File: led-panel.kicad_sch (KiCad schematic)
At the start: 12 parts

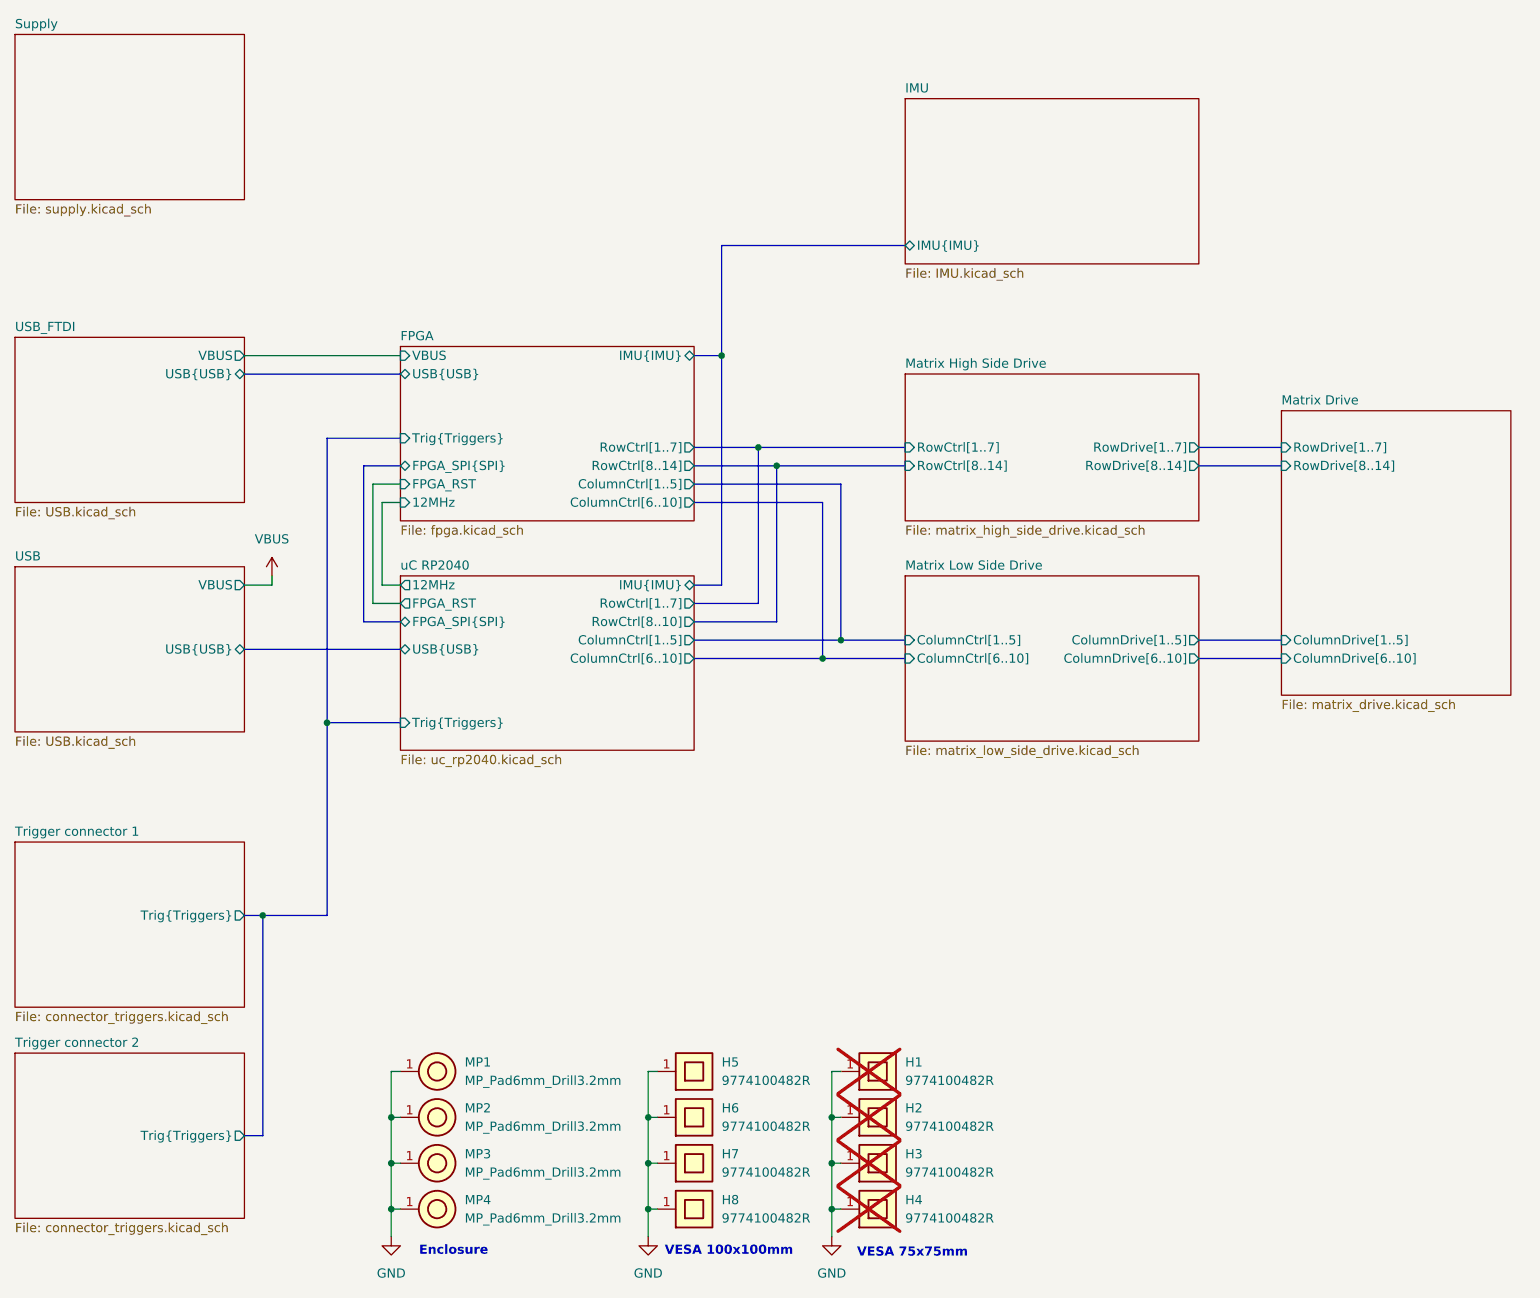
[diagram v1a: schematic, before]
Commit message: [#72133] Update USB FTDI sheet
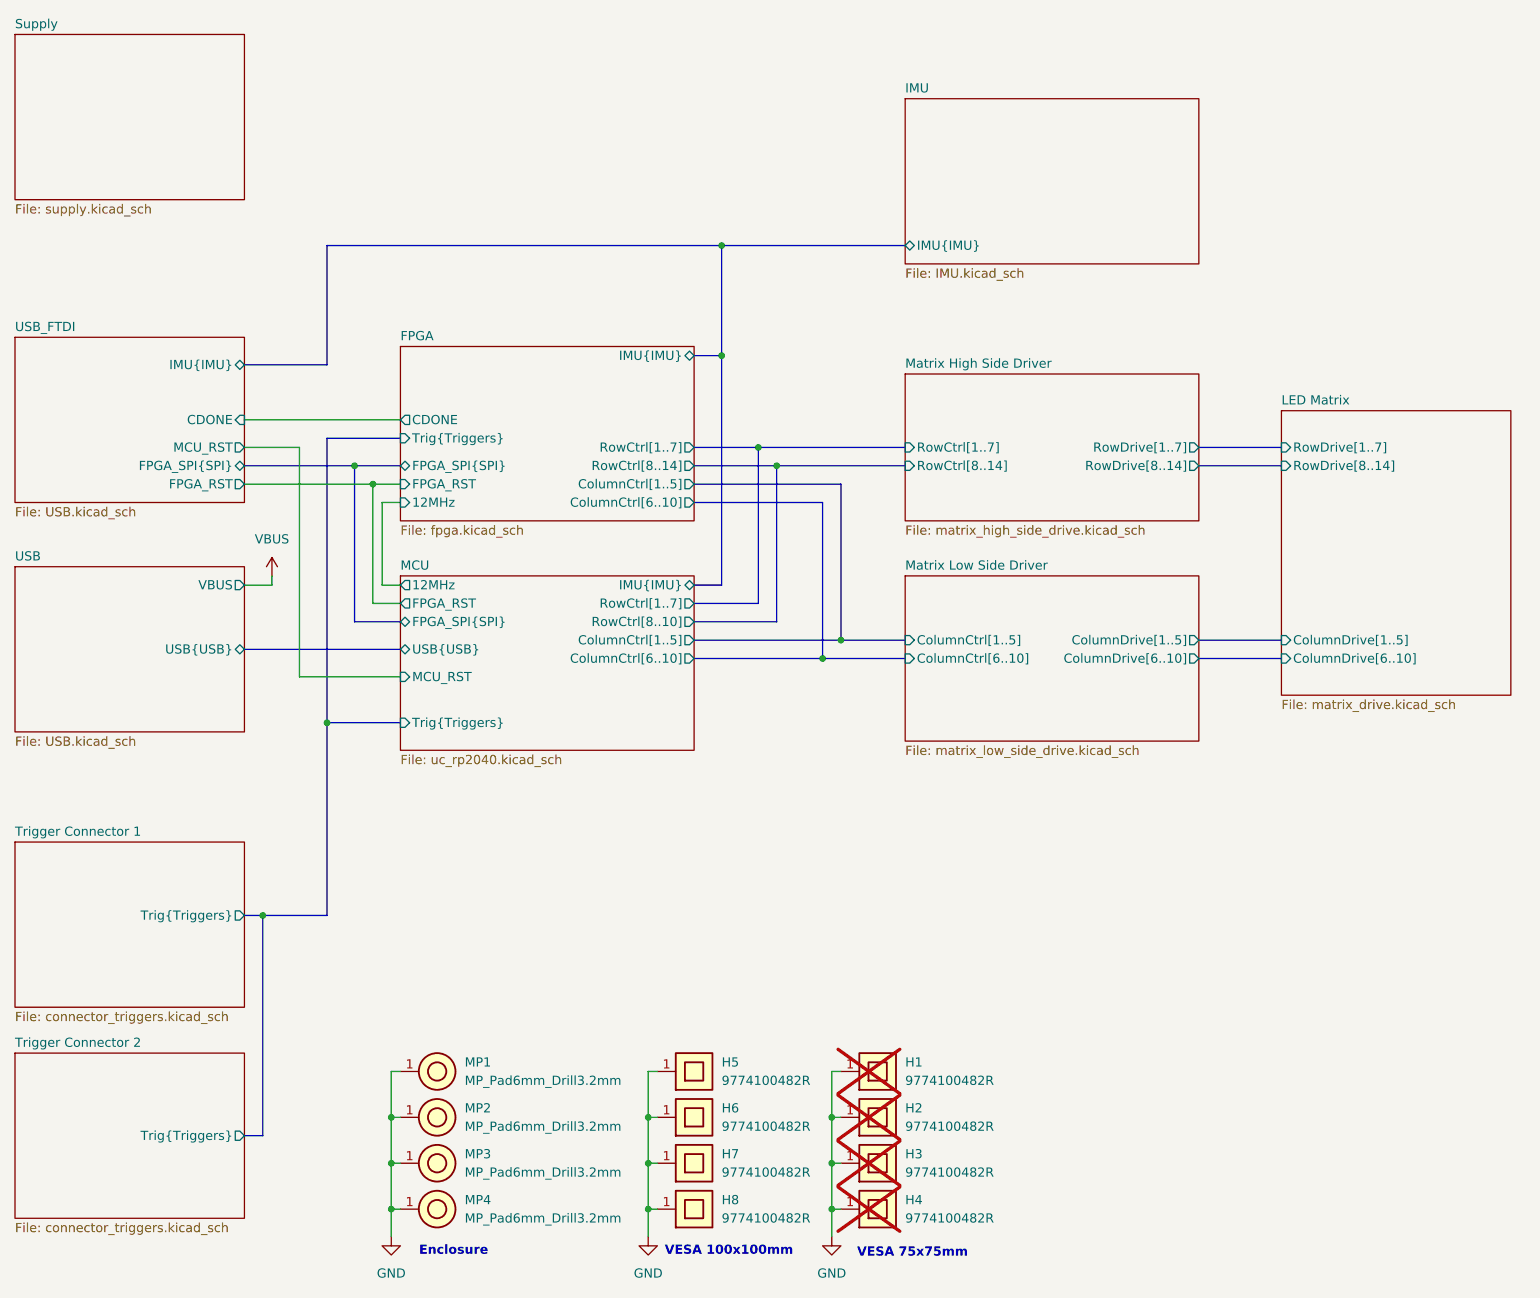
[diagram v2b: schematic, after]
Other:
- sheet Matrix Drive renamed LED Matrix
- sheet Matrix High Side Drive renamed Matrix High Side Driver
- sheet Matrix Low Side Drive renamed Matrix Low Side Driver
- sheet Trigger connector 1 renamed Trigger Connector 1
- sheet Trigger connector 2 renamed Trigger Connector 2
- sheet uC RP2040 renamed MCU
- sheet FPGA ports: added CDONE; removed USB{USB}, VBUS
- sheet MCU ports: added MCU_RST; removed none
- sheet USB_FTDI ports: added CDONE, FPGA_RST, FPGA_SPI{SPI}, IMU{IMU}, MCU_RST; removed USB{USB}, VBUS
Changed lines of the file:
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@@
 	)
 	(junction
+		(at 85.09 82.55)
+		(diameter 0)
+		(color 0 0 0 0)
+	)
+	(junction
+		(at 87.63 85.09)
+		(diameter 0)
+		(color 0 0 0 0)
+	)
+	(junction
 		(at 152.4 106.68)
 		(diameter 0)
@@
 	)
 	(junction
+		(at 135.89 52.07)
+		(diameter 0)
+		(color 0 0 0 0)
+	)
+	(junction
 		(at 125.73 185.42)
 		(diameter 0)
@@
 		)
 	)
+	(bus
+		(pts
+			(xy 69.85 68.58) (xy 81.28 68.58)
+		)
+		(stroke
+			(width 0)
+			(type default)
+		)
+	)
 	(wire
 		(pts
@@
 	(wire
 		(pts
-			(xy 69.85 67.31) (xy 91.44 67.31)
-		)
-		(stroke
-			(width 0)
-			(type default)
-		)
-	)
-	(wire
-		(pts
 			(xy 125.73 179.07) (xy 127 179.07)
 		)
@@
 		)
 	)
+	(wire
+		(pts
+			(xy 69.85 76.2) (xy 91.44 76.2)
+		)
+		(stroke
+			(width 0)
+			(type default)
+		)
+	)
 	(bus
 		(pts
@@
 	(bus
 		(pts
-			(xy 91.44 104.14) (xy 86.36 104.14)
+			(xy 91.44 104.14) (xy 85.09 104.14)
 		)
 		(stroke
@@
 	(bus
 		(pts
+			(xy 81.28 52.07) (xy 135.89 52.07)
+		)
+		(stroke
+			(width 0)
+			(type default)
+		)
+	)
+	(bus
+		(pts
 			(xy 72.39 175.26) (xy 69.85 175.26)
 		)
@@
 	(wire
 		(pts
+			(xy 69.85 85.09) (xy 87.63 85.09)
+		)
+		(stroke
+			(width 0)
+			(type default)
+		)
+	)
+	(wire
+		(pts
 			(xy 151.13 185.42) (xy 151.13 189.23)
 		)
@@
 	(bus
 		(pts
-			(xy 86.36 82.55) (xy 91.44 82.55)
+			(xy 85.09 82.55) (xy 91.44 82.55)
 		)
 		(stroke
@@
 	(wire
 		(pts
+			(xy 69.85 80.01) (xy 77.47 80.01)
+		)
+		(stroke
+			(width 0)
+			(type default)
+		)
+	)
+	(wire
+		(pts
+			(xy 77.47 111.76) (xy 91.44 111.76)
+		)
+		(stroke
+			(width 0)
+			(type default)
+		)
+	)
+	(wire
+		(pts
 			(xy 125.73 179.07) (xy 125.73 185.42)
 		)
@@
 		)
 	)
+	(bus
+		(pts
+			(xy 69.85 82.55) (xy 85.09 82.55)
+		)
+		(stroke
+			(width 0)
+			(type default)
+		)
+	)
 	(wire
 		(pts
@@
 	(bus
 		(pts
-			(xy 69.85 69.85) (xy 91.44 69.85)
+			(xy 132.08 67.31) (xy 135.89 67.31)
 		)
 		(stroke
@@
 	(bus
 		(pts
-			(xy 132.08 67.31) (xy 135.89 67.31)
+			(xy 85.09 104.14) (xy 85.09 82.55)
+		)
+		(stroke
+			(width 0)
+			(type default)
+		)
+	)
+	(wire
+		(pts
+			(xy 77.47 80.01) (xy 77.47 111.76)
 		)
 		(stroke
@@
 	(bus
 		(pts
-			(xy 86.36 104.14) (xy 86.36 82.55)
+			(xy 81.28 68.58) (xy 81.28 52.07)
 		)
 		(stroke
@@
 			(color 0 0 0 0.0000)
 		)
-		(property "Sheetname" "uC RP2040"
+		(property "Sheetname" "MCU"
 			(at 91.44 97.0784 0)
 			(effects
@@
 			)
 		)
+		(pin "MCU_RST" input
+			(at 91.44 111.76 180)
+			(effects
+				(font
+					(size 1.27 1.27)
+				)
+				(justify left)
+			)
+		)
 		(instances
 			(project "led-panel"
@@
 			(color 0 0 0 0.0000)
 		)
-		(property "Sheetname" "Trigger connector 2"
+		(property "Sheetname" "Trigger Connector 2"
 			(at 38.1 163.1184 0)
 			(effects
@@
 			(color 0 0 0 0.0000)
 		)
-		(property "Sheetname" "Matrix Drive"
+		(property "Sheetname" "LED Matrix"
 			(at 213.36 74.2184 0)
 			(effects
@@
 			(color 0 0 0 0.0000)
 		)
-		(property "Sheetname" "Trigger connector 1"
+		(property "Sheetname" "Trigger Connector 1"
 			(at 38.1 133.9084 0)
 			(effects
@@
 			(color 0 0 0 0.0000)
 		)
-		(property "Sheetname" "Matrix Low Side Drive"
+		(property "Sheetname" "Matrix Low Side Driver"
 			(at 161.29 97.0784 0)
 			(effects
@@
 			(color 0 0 0 0.0000)
 		)
-		(property "Sheetname" "Matrix High Side Drive"
+		(property "Sheetname" "Matrix High Side Driver"
 			(at 161.29 69.1384 0)
 			(effects
@@
 			)
 		)
-		(pin "USB{USB}" bidirectional
-			(at 69.85 69.85 0)
+		(pin "FPGA_SPI{SPI}" bidirectional
+			(at 69.85 82.55 0)
 			(effects
 				(font
@@
 			)
 		)
-		(pin "VBUS" output
-			(at 69.85 67.31 0)
+		(pin "IMU{IMU}" bidirectional
+			(at 69.85 68.58 0)
+			(effects
+				(font
+					(size 1.27 1.27)
+				)
+				(justify right)
+			)
+		)
+		(pin "FPGA_RST" output
+			(at 69.85 85.09 0)
+			(effects
+				(font
+					(size 1.27 1.27)
+				)
+				(justify right)
+			)
+		)
+		(pin "MCU_RST" output
+			(at 69.85 80.01 0)
+			(effects
+				(font
+					(size 1.27 1.27)
+				)
+				(justify right)
+			)
+		)
+		(pin "CDONE" input
+			(at 69.85 76.2 0)
 			(effects
 				(font
@@
 			)
 		)
-		(pin "USB{USB}" bidirectional
-			(at 91.44 69.85 180)
-			(effects
-				(font
-					(size 1.27 1.27)
-				)
-				(justify left)
-			)
-		)
 		(pin "12MHz" input
 			(at 91.44 87.63 180)
@@
 			)
 		)
-		(pin "VBUS" input
-			(at 91.44 67.31 180)
+		(pin "FPGA_RST" input
+			(at 91.44 85.09 180)
 			(effects
 				(font
@@
 			)
 		)
-		(pin "FPGA_RST" input
-			(at 91.44 85.09 180)
+		(pin "FPGA_SPI{SPI}" bidirectional
+			(at 91.44 82.55 180)
 			(effects
 				(font
@@
 			)
 		)
-		(pin "FPGA_SPI{SPI}" bidirectional
-			(at 91.44 82.55 180)
+		(pin "CDONE" output
+			(at 91.44 76.2 180)
 			(effects
 				(font

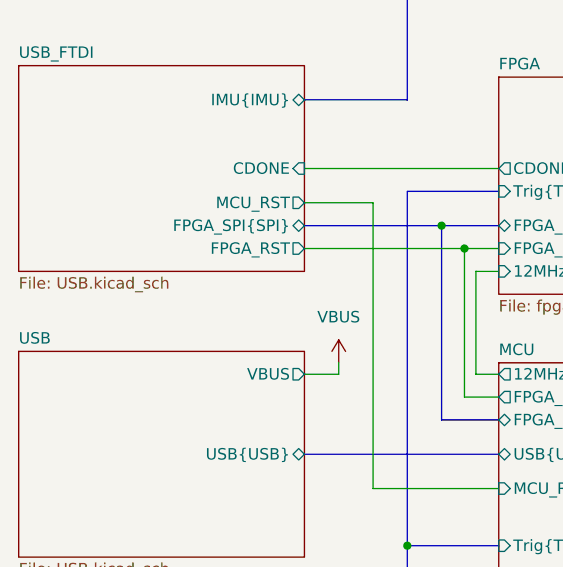
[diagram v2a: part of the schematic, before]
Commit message: [#72133] Update USB sheets
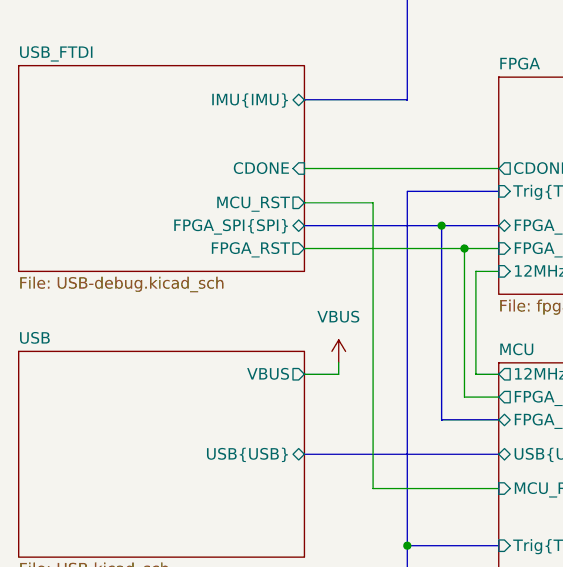
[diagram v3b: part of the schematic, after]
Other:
- sheet USB_FTDI: file USB.kicad_sch -> USB-debug.kicad_sch
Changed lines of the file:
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@@
 			)
 		)
-		(property "Sheetfile" "USB.kicad_sch"
+		(property "Sheetfile" "USB-debug.kicad_sch"
 			(at 38.1 88.2146 0)
 			(effects

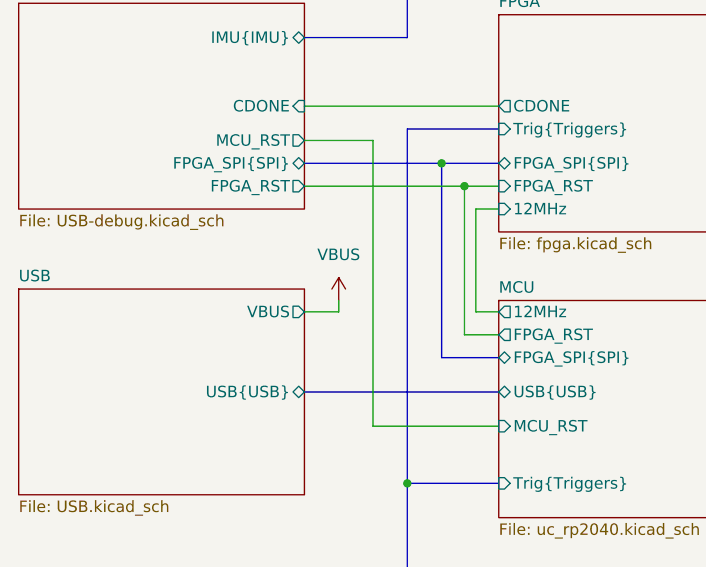
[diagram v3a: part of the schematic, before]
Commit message: [#72133] Add captions to schematic sheets
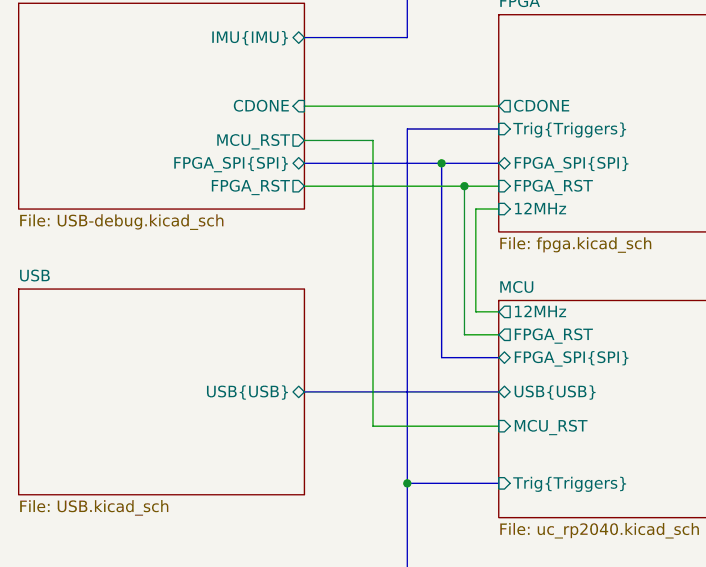
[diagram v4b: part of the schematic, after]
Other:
- sheet USB ports: added none; removed VBUS

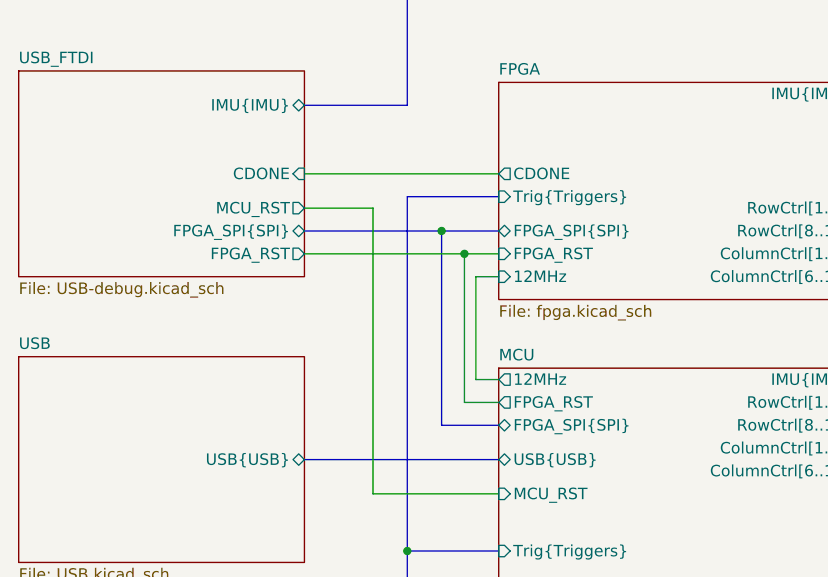
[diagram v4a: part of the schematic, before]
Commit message: [#72133] Clean ERC
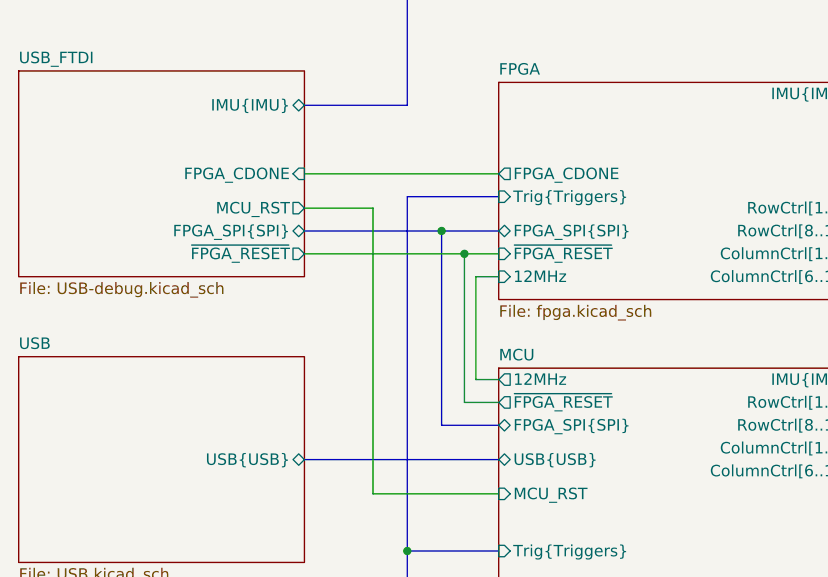
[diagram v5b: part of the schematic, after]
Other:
- sheet FPGA ports: added FPGA_CDONE, ~{FPGA_RESET}; removed CDONE, FPGA_RST
- sheet MCU ports: added ~{FPGA_RESET}; removed FPGA_RST
- sheet USB_FTDI ports: added FPGA_CDONE, ~{FPGA_RESET}; removed CDONE, FPGA_RST
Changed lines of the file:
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@@
-			)
-		)
-		(pin "FPGA_RST" output
-			(at 91.44 101.6 180)
-			(effects
-				(font
-					(size 1.27 1.27)
-				)
-				(justify left)
 			)
 		)
@@
 			)
 		)
+		(pin "~{FPGA_RESET}" output
+			(at 91.44 101.6 180)
+			(effects
+				(font
+					(size 1.27 1.27)
+				)
+				(justify left)
+			)
+		)
 		(instances
 			(project "led-panel"
@@
 			)
 		)
-		(pin "FPGA_RST" output
-			(at 69.85 85.09 0)
-			(effects
-				(font
-					(size 1.27 1.27)
-				)
-				(justify right)
-			)
-		)
 		(pin "MCU_RST" output
 			(at 69.85 80.01 0)
@@
 			)
 		)
-		(pin "CDONE" input
+		(pin "FPGA_CDONE" input
 			(at 69.85 76.2 0)
+			(effects
+				(font
+					(size 1.27 1.27)
+				)
+				(justify right)
+			)
+		)
+		(pin "~{FPGA_RESET}" output
+			(at 69.85 85.09 0)
 			(effects
 				(font
@@
 			)
 		)
-		(pin "FPGA_RST" input
-			(at 91.44 85.09 180)
-			(effects
-				(font
-					(size 1.27 1.27)
-				)
-				(justify left)
-			)
-		)
 		(pin "FPGA_SPI{SPI}" bidirectional
 			(at 91.44 82.55 180)
@@
 			)
 		)
-		(pin "CDONE" output
+		(pin "FPGA_CDONE" output
 			(at 91.44 76.2 180)
 			(effects
 				(font
+					(size 1.27 1.27)
+				)
+				(justify left)
+			)
+		)
+		(pin "~{FPGA_RESET}" input
+			(at 91.44 85.09 180)
+			(effects
+				(font
